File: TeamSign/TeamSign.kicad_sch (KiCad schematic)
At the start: 48 parts, among them J1 RJ45, J2 Barrel_Jack_MountingPin, Q1 BSS138, Q2 BSS138, U1 TPS563200, U2 ESP32-Devkit_C_V4

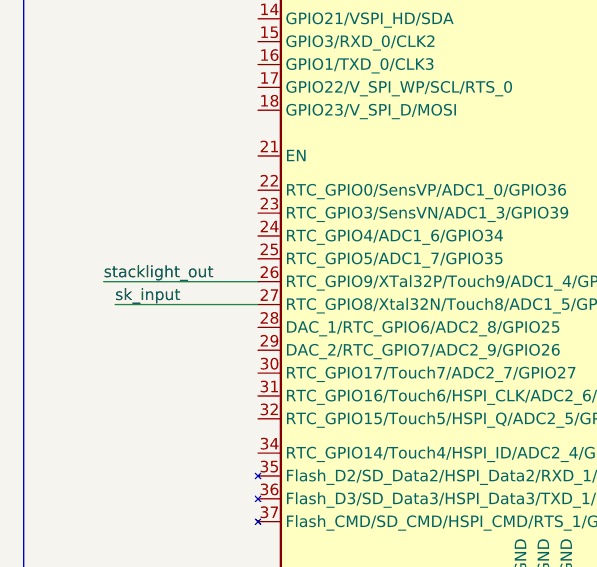
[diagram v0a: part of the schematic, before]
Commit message: Move connectors to front of board so they're in the bulky area.
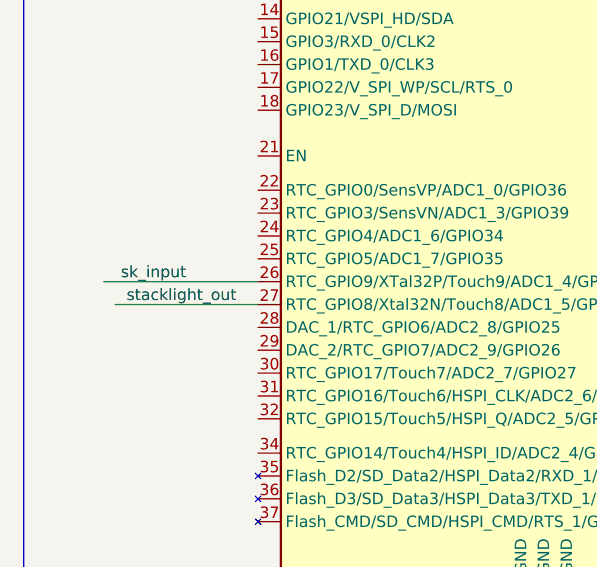
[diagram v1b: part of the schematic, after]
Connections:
- net sk_input: now also U2.26 (RTC_GPIO9/XTal32P/Touch9/ADC1_4/GPIO32); no longer U2.27 (RTC_GPIO8/Xtal32N/Touch8/ADC1_5/GPIO33)
- net stacklight_out: now also U2.27 (RTC_GPIO8/Xtal32N/Touch8/ADC1_5/GPIO33); no longer U2.26 (RTC_GPIO9/XTal32P/Touch9/ADC1_4/GPIO32)
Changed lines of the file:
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@@
     (effects (font (size 1.27 1.27)) (justify left bottom))
   )
-  (label "sk_input" (at 26.67 210.185 0) (fields_autoplaced)
+  (label "sk_input" (at 27.305 207.645 0) (fields_autoplaced)
     (effects (font (size 1.27 1.27)) (justify left bottom))
   )
@@
     (effects (font (size 1.27 1.27)) (justify left bottom))
   )
-  (label "stacklight_out" (at 25.4 207.645 0) (fields_autoplaced)
+  (label "stacklight_out" (at 27.94 210.185 0) (fields_autoplaced)
     (effects (font (size 1.27 1.27)) (justify left bottom))
   )

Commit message: Updated link, BOM, and some general sanity changes.
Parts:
- renumbered C98 to C9999
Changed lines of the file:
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@@
   (symbol (lib_id "Device:C") (at 187.325 272.415 0) (unit 1)
     (in_bom no) (on_board no) (dnp yes) (fields_autoplaced)
-    (property "Reference" "C98" (at 191.135 271.78 0)
+    (property "Reference" "C9999" (at 191.135 271.78 0)
       (effects (font (size 1.27 1.27)) (justify left))
     )
@@
       (project "TeamSign"
         (path "/e53f9913-0070-41c4-b6c8-5a044462b6d9"
-          (reference "C98") (unit 1)
+          (reference "C9999") (unit 1)
         )
       )
